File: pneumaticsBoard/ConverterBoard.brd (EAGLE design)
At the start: 82.5 x 69.5 mm, 26 parts, among them IC1 MAX232, Q1 2N3819, Q2 2N3819, Q3 2N3819, Q4 2N3819, Q5 2N3819, Q6 2N3819, Q7 2N3819, Q8 2N3819, U1 ATMEGA328P-PU, X1 5566-4

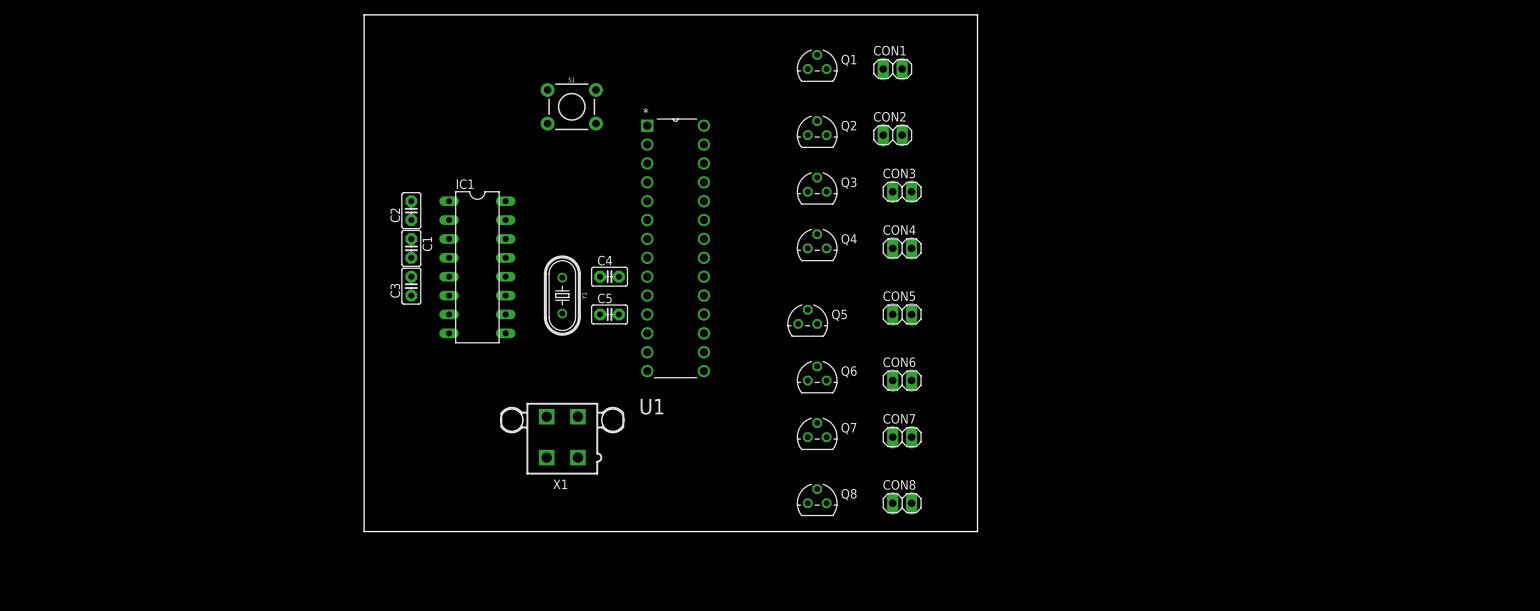
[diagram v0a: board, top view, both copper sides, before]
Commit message: Added 12V-5V Con. Q needs attention. Layout changed to 1x6 rect.
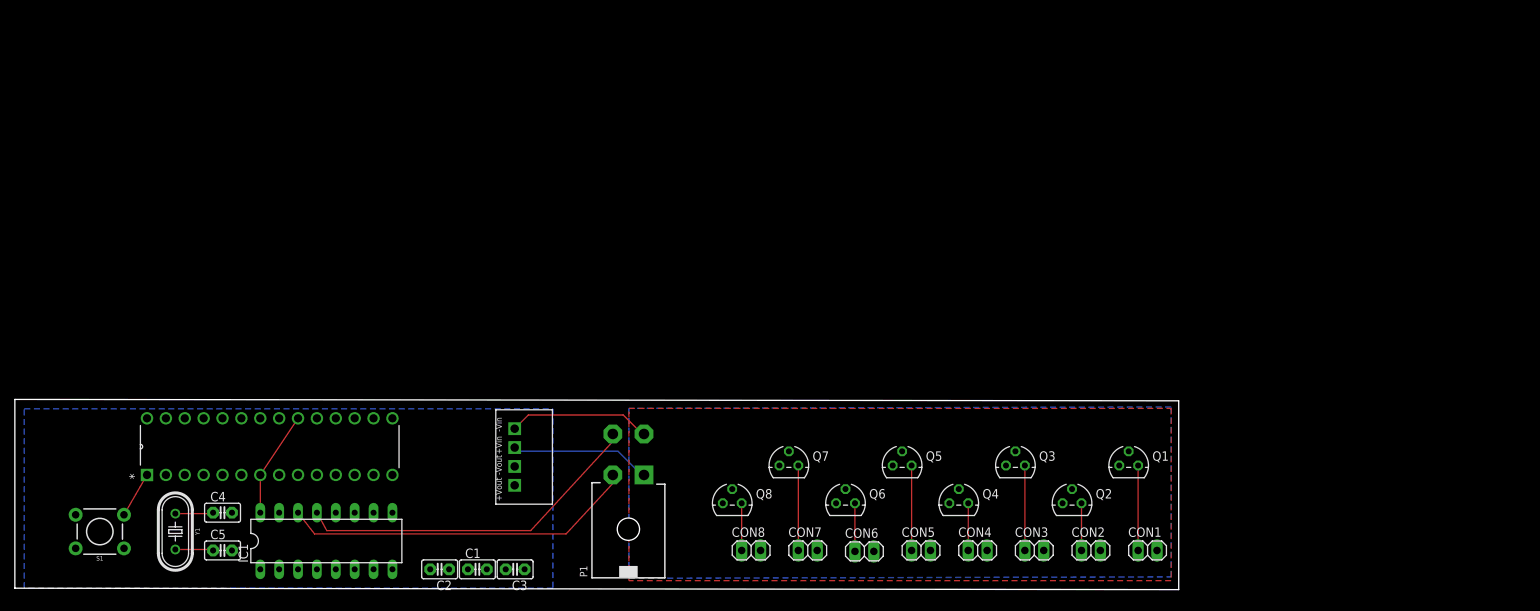
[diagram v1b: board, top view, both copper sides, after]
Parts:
- removed X1: 5566-4, con-molex:5566-4
- added P1: 39-30-04?_S, con-molex-mini-fit:39-30-?04?
- added U$1: CRL2S1205SC, CRL2S1205SC:CRL2S1205SC
- moved S1 85.4 mm to (11.4, 7.62), turned to 180 degrees
- moved CON1 73.3 mm to (152.4, 5.08)
- moved Q1 67.8 mm to (149.9, 16.5)
- moved CON2 61.9 mm to (144.8, 5.08)
- moved C4 61.0 mm to (27.9, 10.2)
- moved C5 61.0 mm to (27.9, 5.08)
- moved Y1 61.0 mm to (21.6, 7.62)
- moved Q2 60.2 mm to (142.2, 11.4)
- moved CON3 51.4 mm to (137.2, 5.08)
- moved C2 48.4 mm to (57.1, 2.54), turned to 180 degrees
- moved Q3 45.5 mm to (134.6, 16.5)
- moved C1 44.1 mm to (62.2, 2.54), turned to 0 degrees
- moved U1 42.4 mm to (50.8, 22.9), turned to 90 degrees
- moved IC1 42.1 mm to (41.9, 6.35), turned to 0 degrees
- moved CON4 41.9 mm to (129.5, 5.08)
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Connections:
- removed net N$25: IC1.13, X1.2
- removed net N$26: IC1.14, X1.3
- new net RX: IC1.13, P1.4
- new net TX: IC1.14, P1.2
- new net VSS: CON1.2, CON2.2, CON3.2, CON4.2, CON5.2, CON6.2, CON7.2, CON8.2, P1.1, U$1.P2
- net GND: now also U$1.P4; no longer CON1.2, CON2.2, CON3.2, CON4.2, CON5.2, CON6.2, CON7.2, CON8.2, X1.1
- net VCC: now also U$1.P3
- net VDD: now also P1.3, U$1.P1; no longer X1.4
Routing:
- net TX: track 0.00 -> 47.9 mm
- net RX: track 0.00 -> 47.5 mm
- net VDD: track 0.00 -> 19.2 mm
- net VSS: track 0.00 -> 18.9 mm
- net VCC: track 0.00 -> 14.2 mm
- net N$23: track 0.00 -> 11.4 mm
- net N$21: track 0.00 -> 11.4 mm
- net N$19: track 0.00 -> 11.4 mm
- net N$15: track 0.00 -> 11.4 mm
- net N$18: track 0.00 -> 6.48 mm
- net N$24: track 0.00 -> 6.35 mm
- net N$22: track 0.00 -> 6.35 mm
- net N$20: track 0.00 -> 6.35 mm
- net RESET: track 0.00 -> 6.19 mm
- net N$16: track 0.00 -> 5.13 mm
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- added copper zone on layer 16, net GND
- added copper zone on layer 1, net VDD
- added copper zone on layer 16, net VSS
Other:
- board size 82.5 x 69.5 mm -> 156.6 x 25.6 mm

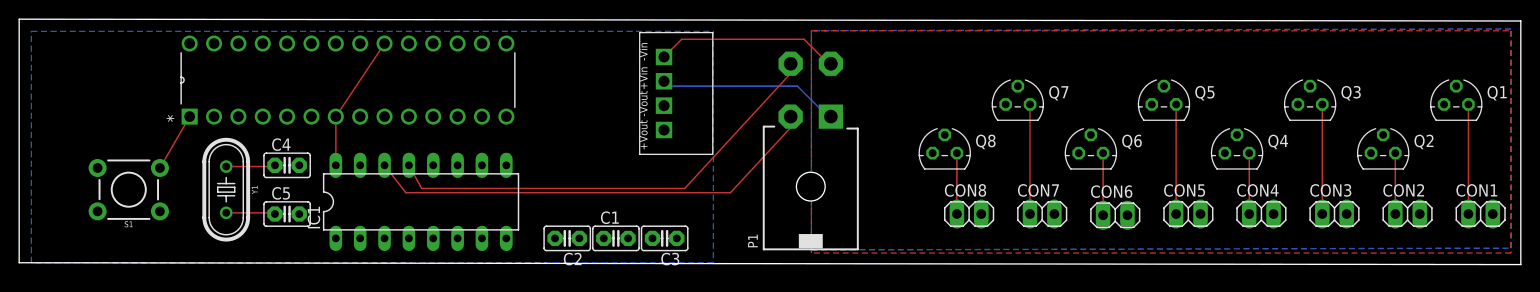
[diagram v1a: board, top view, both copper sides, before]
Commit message: Pneumatics update - something incorrect with EAGLE GND planes
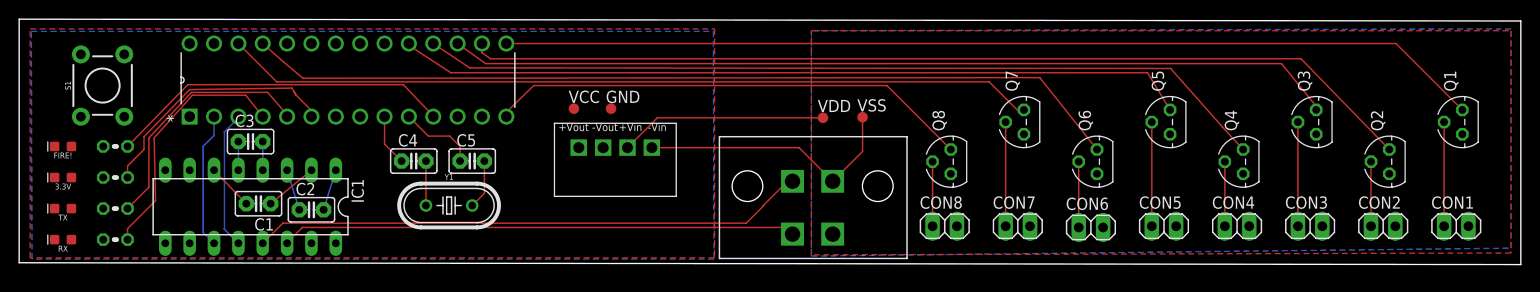
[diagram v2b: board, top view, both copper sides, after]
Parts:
- removed P1: 39-30-04?_S, con-molex-mini-fit:39-30-?04?
- added 3.3V, FIRE!, RX, TX: BLUE, SparkFun-LED:LED-0603
- added GND, VCC, VDD, VSS: TPTP11R, testpad:TP11R
- added R1, R2, R3, R5: (no value), resistor:0204V
- added U$2: MINI_FIT_JR_4PIN_VERT, 15-24-6041:MINI_FIT_JR_4PIN_VERT
- Q1, Q2, Q3, Q4, Q5, Q6, Q7, Q8: value 2N3819 -> BSS296
- moved C3 44.3 mm to (24.1, 12.6), turned to 0 degrees
- moved C1 37.4 mm to (25.0, 6.16), turned to 180 degrees
- moved C2 26.8 mm to (30.5, 5.52), turned to 0 degrees
- moved Y1 23.3 mm to (44.8, 5.97), turned to 0 degrees
- moved C5 20.1 mm to (47.2, 10.6)
- moved IC1 17.8 mm to (24.1, 5.84), turned to 180 degrees
- moved C4 13.2 mm to (41.1, 10.6)
- moved U$1 12.6 mm to (66.0, 9.46), turned to 180 degrees
- moved S1 11.2 mm to (8.70, 18.5), turned to 90 degrees
- moved CON5 2.84 mm to (119.4, 3.81)
- moved CON7 2.84 mm to (104.1, 3.81)
- moved CON8 2.84 mm to (96.5, 3.81)
- moved CON1 2.84 mm to (149.9, 3.81)
- moved CON2 2.84 mm to (142.2, 3.81)
- moved CON3 2.84 mm to (134.6, 3.81)
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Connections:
- removed net N$3: Q2.2, U1.15
- removed net N$4: Q3.2, U1.16
- removed net N$5: Q4.2, U1.17
- removed net N$6: Q5.2, U1.18
- removed net SCL: U1.28
- removed net SDA: U1.27
- new net N$25: R5.2, U1.11
- new net POWER: 3.3V.A, R3.1
- new net Q1: Q1.1, U1.15
- new net Q2: Q2.1, U1.16
- new net Q3: Q3.1, U1.17
- new net Q4: Q4.1, U1.18
- new net Q5: Q5.1, U1.19
- new net Q6: Q6.1, U1.25
- new net Q7: Q7.1, U1.26
- new net Q8: Q8.1, U1.14
- new net RX_ON: R1.1, RX.A
- new net TX_ON: R2.1, TX.A
- net GND: now also 3.3V.C, FIRE!.C, GND.TP, RX.C, TX.C, U$1.P3; no longer U$1.P4
- net N$1: now also R3.2, U1.6; no longer Q7.2, U1.26
- net N$15: now also CON8.1, Q8.2; no longer CON5.1, Q5.1
- net N$18: now also CON1.1, Q1.2; no longer CON6.1, Q6.1
- net N$19: now also CON2.1, Q2.2; no longer CON1.1, Q1.1
- net N$2: now also FIRE!.A, R5.1; no longer Q1.2, U1.14
- net N$20: now also CON3.1, Q3.2; no longer CON2.1, Q2.1
- net N$21: now also CON4.1, Q4.2; no longer CON3.1, Q3.1
- net N$22: now also CON5.1, Q5.2; no longer CON4.1, Q4.1
- net N$23: now also Q7.2; no longer Q7.1
- net N$24: now also CON6.1, Q6.2; no longer CON8.1, Q8.1
- net N$7: now also R1.2, U1.4; no longer Q6.2, U1.19
- net N$8: now also R2.2, U1.5; no longer Q8.2, U1.25
- net RX: now also U$2.P3; no longer P1.4
- net TX: now also U$2.P1; no longer P1.2
- net VCC: now also U$1.P4, VCC.TP; no longer U$1.P3
- net VDD: now also U$1.P2, U$2.P2, VDD.TP; no longer P1.3, U$1.P1
- net VSS: now also U$1.P1, U$2.P4, VSS.TP; no longer P1.1, U$1.P2
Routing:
- net Q1: track 0.00 -> 102.6 mm
- net Q2: track 0.00 -> 99.8 mm
- net Q3: track 0.00 -> 92.7 mm
- net Q6: track 0.00 -> 92.0 mm
- net Q4: track 0.00 -> 89.0 mm
- net Q7: track 0.00 -> 84.8 mm
- net Q5: track 0.00 -> 82.6 mm
- net Q8: track 0.00 -> 50.7 mm
- net N$25: track 0.00 -> 36.1 mm
- net N$1: track 0.00 -> 26.7 mm
- net N$7: track 0.00 -> 26.2 mm
- net N$8: track 0.00 -> 26.0 mm
- net RS232_RX-ATMEGA_TX: track 0.00 -> 14.4 mm
- net VCC: track 14.2 -> 0.00 mm
- net RS232_TX-ATMEGA_RX: track 0.00 -> 14.2 mm
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- added copper zone on layer 1, net VCC

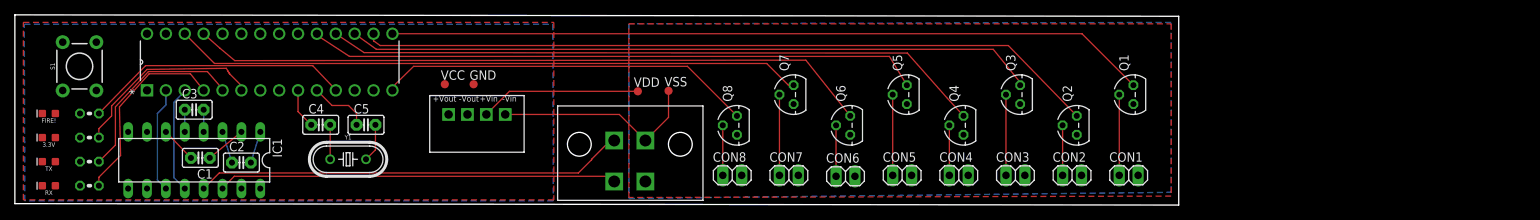
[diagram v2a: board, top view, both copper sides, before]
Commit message: Added Blaine's acoustics .sch - pneu almost done except for orphan adjustment
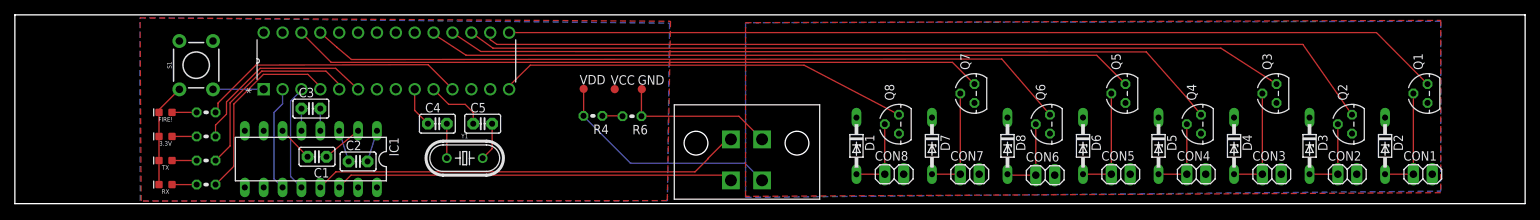
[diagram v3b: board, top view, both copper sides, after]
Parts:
- removed U$1: CRL2S1205SC, CRL2S1205SC:CRL2S1205SC
- removed VSS: TPTP11R, testpad:TP11R
- added D1, D2, D3, D4, D5, D6, D7, D8: BZX90, diode:DO34Z7
- added R4, R6: (no value), resistor:0204V
- moved CON1 39.6 mm to (189.4, 3.96)
- moved Q1 39.6 mm to (190.1, 14.8)
- moved CON2 37.0 mm to (179.3, 3.96)
- moved Q2 37.0 mm to (179.9, 10.7)
- moved CON3 34.5 mm to (169.1, 3.96)
- moved Q3 34.5 mm to (169.7, 14.8)
- moved CON4 32.0 mm to (159.0, 3.96)
- moved Q4 32.0 mm to (159.6, 10.7)
- moved CON5 29.4 mm to (148.8, 3.96)
- moved Q5 29.4 mm to (149.4, 14.8)
- moved Q6 26.9 mm to (139.3, 10.7)
- moved CON6 26.9 mm to (138.6, 3.84)
- moved Q7 24.3 mm to (129.1, 14.8)
- moved CON7 24.3 mm to (128.5, 3.96)
- moved VCC 22.9 mm to (80.7, 15.4)
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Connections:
- removed net N$15: CON8.1, Q8.2
- removed net N$18: CON1.1, Q1.2
- removed net N$19: CON2.1, Q2.2
- removed net N$20: CON3.1, Q3.2
- removed net N$21: CON4.1, Q4.2
- removed net N$22: CON5.1, Q5.2
- removed net N$23: CON7.1, Q7.2
- removed net N$24: CON6.1, Q6.2
- removed net VSS: CON1.2, CON2.2, CON3.2, CON4.2, CON5.2, CON6.2, CON7.2, CON8.2, U$1.P1, U$2.P4, VSS.TP
- new net CON1_GND: CON1.1, D2.A, Q1.2
- new net CON2_GND: CON2.1, D3.A, Q2.2
- new net CON3_GND: CON3.1, D4.A, Q3.2
- new net CON4_GND: CON4.1, D5.A, Q4.2
- new net CON5_GND: CON5.1, D6.A, Q5.2
- new net CON6_GND: CON6.1, D8.A, Q6.2
- new net CON7_GND: CON7.1, D7.A, Q7.2
- new net CON8_GND: CON8.1, D1.A, Q8.2
- new net N$3: R4.1, R6.2
- net GND: now also Q1.3, Q2.3, Q3.3, Q4.3, Q5.3, Q6.3, Q7.3, Q8.3, R6.1, U$2.P4; no longer U$1.P3
- net VCC: no longer U$1.P4
- net VDD: now also CON1.2, CON2.2, CON3.2, CON4.2, CON5.2, CON6.2, CON7.2, CON8.2, D1.C, D2.C, D3.C, D4.C, D5.C, D6.C, D7.C, D8.C, R4.2; no longer Q1.3, Q2.3, Q3.3, Q4.3, Q5.3, Q6.3, Q7.3, Q8.3, U$1.P2
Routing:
- net GND: track 0.00 -> 35.1 mm
- net VSS: track 28.3 -> 0.00 mm
- net Q1: track 102.6 -> 126.5 mm
- net Q2: track 99.8 -> 122.0 mm
- net Q3: track 92.7 -> 110.4 mm
- net Q4: track 89.0 -> 105.3 mm
- net CON7_GND: track 0.00 -> 14.7 mm
- net CON5_GND: track 0.00 -> 14.7 mm
- net CON3_GND: track 0.00 -> 14.7 mm
- net CON1_GND: track 0.00 -> 14.7 mm
- net Q5: track 82.6 -> 95.7 mm
- net Q6: track 92.0 -> 102.9 mm
- net N$23: track 10.9 -> 0.00 mm
- net N$22: track 10.9 -> 0.00 mm
- net N$20: track 10.9 -> 0.00 mm
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- removed copper zone on layer 16, net VSS
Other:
- board size 156.6 x 25.6 mm -> 203.2 x 25.4 mm

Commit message: Finished Pneumatics Board, if RS232 still exists in a day
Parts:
- removed C2, C3, C4, C5: (no value), capacitor-wima:C2.5-2
- added C10, C8, C9: 1uF, SparkFun-Capacitors:0603
- added C6: 22pF, SparkFun-Capacitors:0603
- added PRESSURE: (no value), con-lstb:MA03-1
- C1: value (none) -> 22pF; device capacitor-wima:C2.5-2 -> SparkFun-Capacitors:0603
- R4: value (none) -> 4.7 K
- R6: value (none) -> 3.3 K
- Y1: value (none) -> 16 MHz
- moved Y1 13.3 mm to (47.3, 7.16)
- moved VCC 13.2 mm to (69.9, 7.86)
- moved VDD 13.1 mm to (65.8, 7.86)
- moved GND 13.1 mm to (73.6, 7.86)
- moved U1 10.9 mm to (55.8, 21.1)
- moved CON5 10.7 mm to (138.1, 3.99)
- moved Q7 10.7 mm to (118.4, 14.8)
- moved U$2 10.7 mm to (85.6, 3.16)
- moved 3.3V 10.7 mm to (9.58, 9.07)
- moved FIRE! 10.7 mm to (9.58, 12.3)
- moved RX 10.7 mm to (9.58, 2.59)
- moved TX 10.7 mm to (9.58, 5.83)
- moved R1 10.7 mm to (15.0, 2.59)
- moved R2 10.7 mm to (15.0, 5.83)
- moved R3 10.7 mm to (15.0, 9.07)
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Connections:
- removed net N$16: C4.2, Y1.1
- removed net N$17: C5.2, Y1.2
- removed net N$25: R5.2, U1.11
- new net N$15: C1.2, Y1.1
- new net N$4: R5.2, U1.24
- new net N$5: C6.2, Y1.2
- new net N$6: PRESSURE.1, U1.11
- net GND: now also PRESSURE.3
- net N$10: now also C9.1; no longer C3.2
- net N$11: now also C8.2; no longer C2.1
- net N$12: now also C9.2; no longer C3.1
- net N$13: now also C10.2; no longer C1.1
- net N$14: now also C10.1; no longer C1.2
- net N$9: now also C8.1; no longer C2.2
- net Q1: now also U1.26; no longer U1.15
- net Q2: now also U1.25; no longer U1.16
- net Q3: now also U1.15; no longer U1.17
- net Q4: now also U1.16; no longer U1.18
- net Q5: now also U1.17; no longer U1.19
- net Q6: now also U1.18; no longer U1.25
- net Q7: now also U1.19; no longer U1.26
- net RS232_RX-ATMEGA_TX: now also U1.2; no longer U1.3
- net RS232_TX-ATMEGA_RX: now also U1.3; no longer U1.2
- net VCC: now also PRESSURE.2
- net XTAL1: now also C1.1; no longer C4.1
- net XTAL2: now also C6.1; no longer C5.1
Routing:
- net N$25: track 36.4 -> 0.00 mm
- net Q1: track 126.5 -> 155.2 mm
- net Q2: track 122.0 -> 143.8 mm
- net N$4: track 0.00 -> 20.3 mm
- net Q7: track 93.4 -> 75.0 mm
- net Q6: track 102.9 -> 84.5 mm
- net N$6: track 0.00 -> 10.1 mm
- net N$14: track 4.85 -> 11.1 mm
- net Q4: track 105.3 -> 99.4 mm
- net Q5: track 95.7 -> 90.1 mm
- net XTAL2: track 8.15 -> 2.50 mm
- net N$17: track 5.16 -> 0.00 mm
- net Q3: track 110.4 -> 105.3 mm
- net N$5: track 0.00 -> 4.82 mm
- net N$16: track 4.64 -> 0.00 mm
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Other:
- board size 203.2 x 25.4 mm -> 188 x 25.4 mm
- board text added: "-"
- board text added: "ATMEGA 328 PU"
- board text added: "CAM SPICER"
- board text added: "CAPSTONE 2018"
- board text added: "CENTER FOR AUTOMOTIVE RESEARCH"
- board text added: "ERIKA KLEK"
- board text added: "JACK SCHNAIBLE"
- board text added: "LISA D'LIMA"
- board text added: "PEW PEW PEW"
- board text added: "UNDERWATER ROBOTICS"
- board text added: "WEAPONS INITIATION SYSTEM"
